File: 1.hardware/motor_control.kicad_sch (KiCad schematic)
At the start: 88 parts, among them IC3 UCC27712QDRQ1, IC4 UCC27712QDRQ1, IC5 UCC27712QDRQ1, J13 2061-603/998-404, J14 2060-452/998-404, J15 2060-453/998-404, Q1 STL130N6F7, Q2 STL130N6F7, Q3 STL130N6F7, Q4 STL130N6F7, Q5 STL130N6F7, Q6 STL130N6F7

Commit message: 중간 저장
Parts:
- removed R153, R154, R155: 0.01R, Resistor_SMD:R_2512_6332Metric, symbol Device:R_Shunt_US
- added R10, R6, R9: 0.01R, Resistor_SMD:R_2512_6332Metric, symbol Device:R_Small_US
- R135, R137, R139: value 2.2/0.25w -> 2.2/0.125w; footprint Resistor_SMD:R_1206_3216Metric -> Resistor_SMD:R_0805_2012Metric
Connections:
- net GNDPWR: now also R10.2, R6.2, R9.2
- net MOTOR_U_SHUNT_P: now also Q2.1 (S_1), Q2.2 (S_2), Q2.3 (S_3), R6.1
- net MOTOR_V_SHUNT_P: now also Q4.1 (S_1), Q4.2 (S_2), Q4.3 (S_3), R9.1
- net MOTOR_W_SHUNT_P: now also Q6.1 (S_1), Q6.2 (S_2), Q6.3 (S_3), R10.1

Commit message: 중간 저장
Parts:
- removed C109, C110, C111: 22uF/100V, Capacitor_SMD:C_Elec_8x10.2, symbol Device:C_Polarized_Small_US
- removed C86, C87: 47uF/50V, Capacitor_SMD:C_Elec_6.3x7.7, symbol Device:C_Polarized_Small_US
- removed R135, R136, R137, R138, R139, R140: 2.2/0.125w, Resistor_SMD:R_0805_2012Metric, symbol Device:R_Small_US
- C88, C89, C90, C91, C92, C93: value 10uF/25V -> 10uF/50V; footprint Capacitor_SMD:C_Elec_4x5.4 -> Capacitor_SMD:C_1206_3216Metric
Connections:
- net 12V: now also C85.1
- net at D18.1: now also IC4.7 (HO), R143.2
- net at IC4.5 (LO), R144.2: now also D19.1
- net at C88.1, C91.1, C97.1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: no longer C85.1
- net at IC3.5 (LO), R142.2: now also D17.1
- net at IC3.7 (HO), R141.2: now also D16.1
- net at IC5.5 (LO), R146.2: now also D21.1
- net at D20.1: now also IC5.7 (HO), R145.2
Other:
- note added: "10uF/50V CL31A106KBHNNNE"
- moved on the sheet: C85, D16, D17, D18, D19, D20, D21, R123, R124, R125

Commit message: 중간 저장
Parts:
- renumbered C90 to C100, C93 to C101, C99 to C102, C105 to C103, C108 to C104, C96 to C105, C102 to C106, C88 to C84, C91 to C85, C97 to C86, C85 to C87, C84 to C88, C103 to C89, C106 to C90, C94 to C91, C100 to C92, C89 to C93, C92 to C94, C98 to C95, C104 to C96, C107 to C97, C95 to C98, C101 to C99, D13 to D12, D16 to D13, D17 to D14, D14 to D15, D18 to D16, D19 to D17, D15 to D18, D20 to D19, D21 to D20, IC3 to IC4, IC4 to IC5, IC5 to IC6, R123 to R119, R132 to R120, R141 to R121, R147 to R122, R126 to R123, R127 to R124, R142 to R125, R148 to R126, R6 to R127, R124 to R128, R133 to R129, R143 to R130, R149 to R131, R128 to R132, R129 to R133, R144 to R134, R150 to R135, R9 to R136, R125 to R137, R134 to R138, R145 to R139, R151 to R140, R130 to R141, R131 to R142, R146 to R143, R152 to R144, R10 to R145, TP12 to TP10, TP14 to TP11, TP11 to TP12, TP15 to TP14, TP10 to TP9

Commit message: 오류 일단 다 잡음
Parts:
- R120, R129, R138: footprint Resistor_SMD:R_0805_2012Metric -> Resistor_SMD:R_1206_3216Metric
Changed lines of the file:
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@@
 			)
 		)
-		(property "Footprint" "Resistor_SMD:R_0805_2012Metric"
+		(property "Footprint" "Resistor_SMD:R_1206_3216Metric"
 			(at 213.36 186.69 0)
 			(effects
@@
 			)
 		)
-		(property "Footprint" "Resistor_SMD:R_0805_2012Metric"
+		(property "Footprint" "Resistor_SMD:R_1206_3216Metric"
 			(at 213.36 110.49 0)
 			(effects
@@
 			)
 		)
-		(property "Footprint" "Resistor_SMD:R_0805_2012Metric"
+		(property "Footprint" "Resistor_SMD:R_1206_3216Metric"
 			(at 212.09 33.02 0)
 			(effects

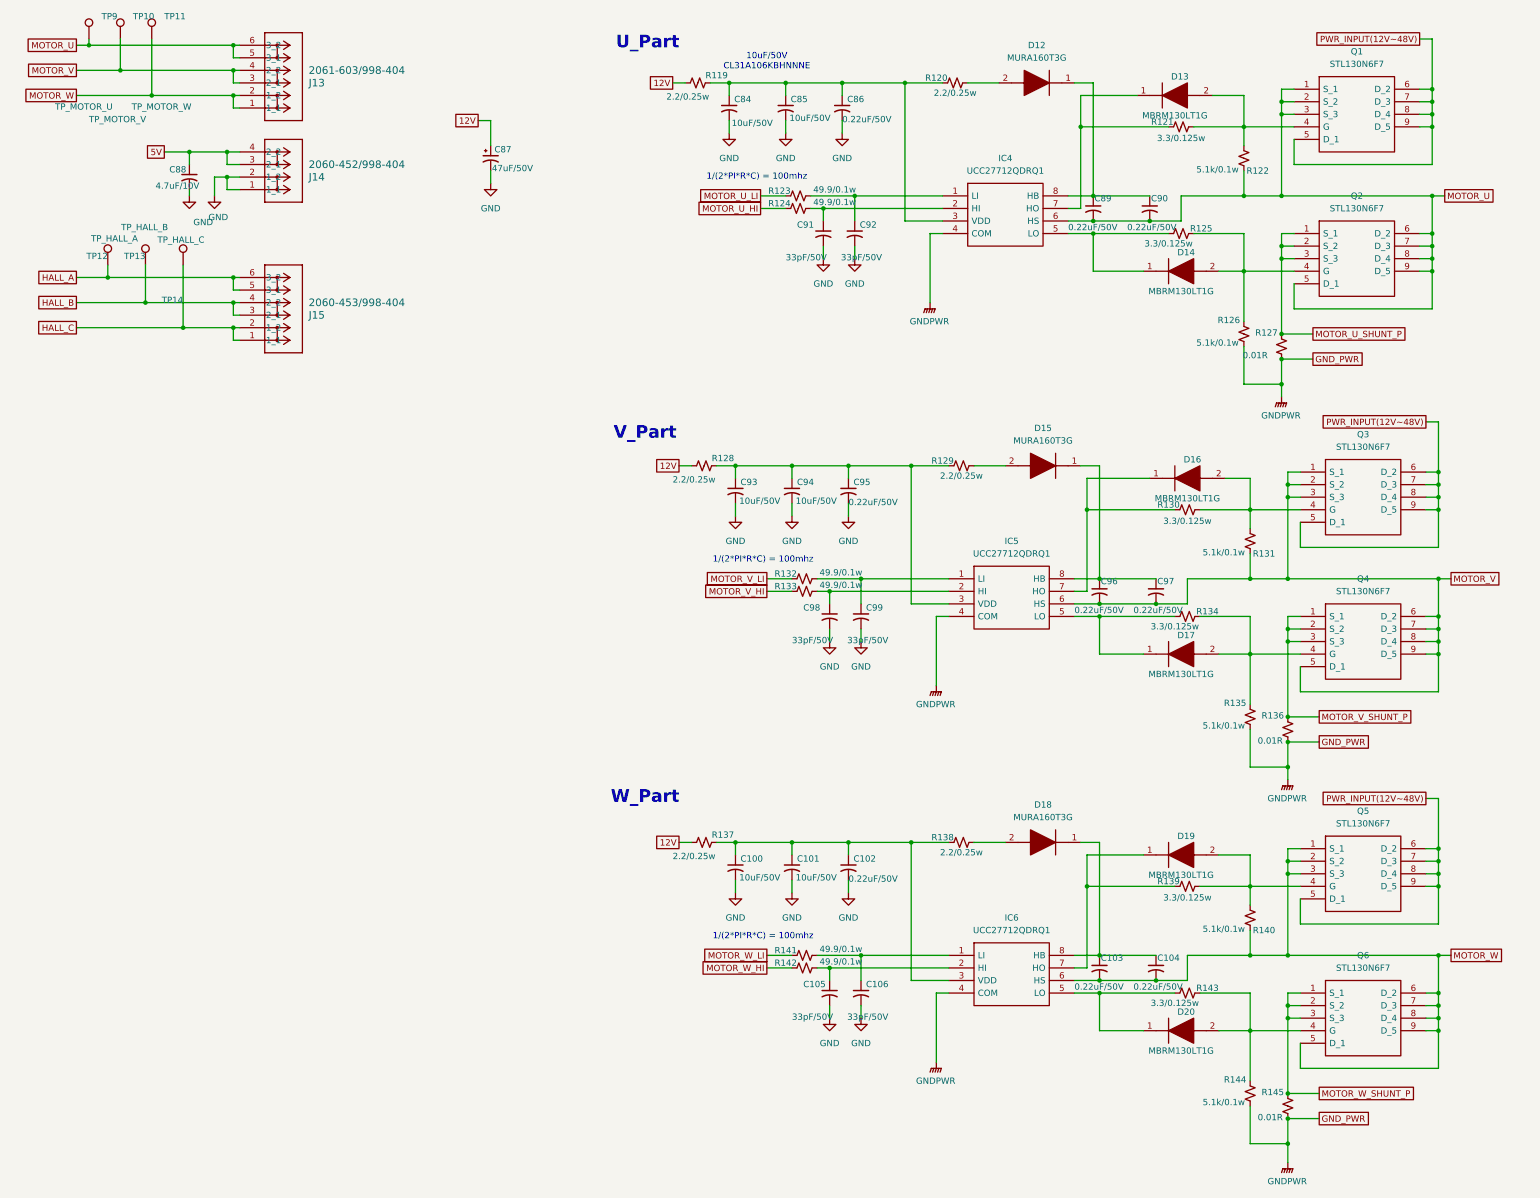
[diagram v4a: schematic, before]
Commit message: 부품 통일 및 필터 부분 캡 선정등 필요해보임
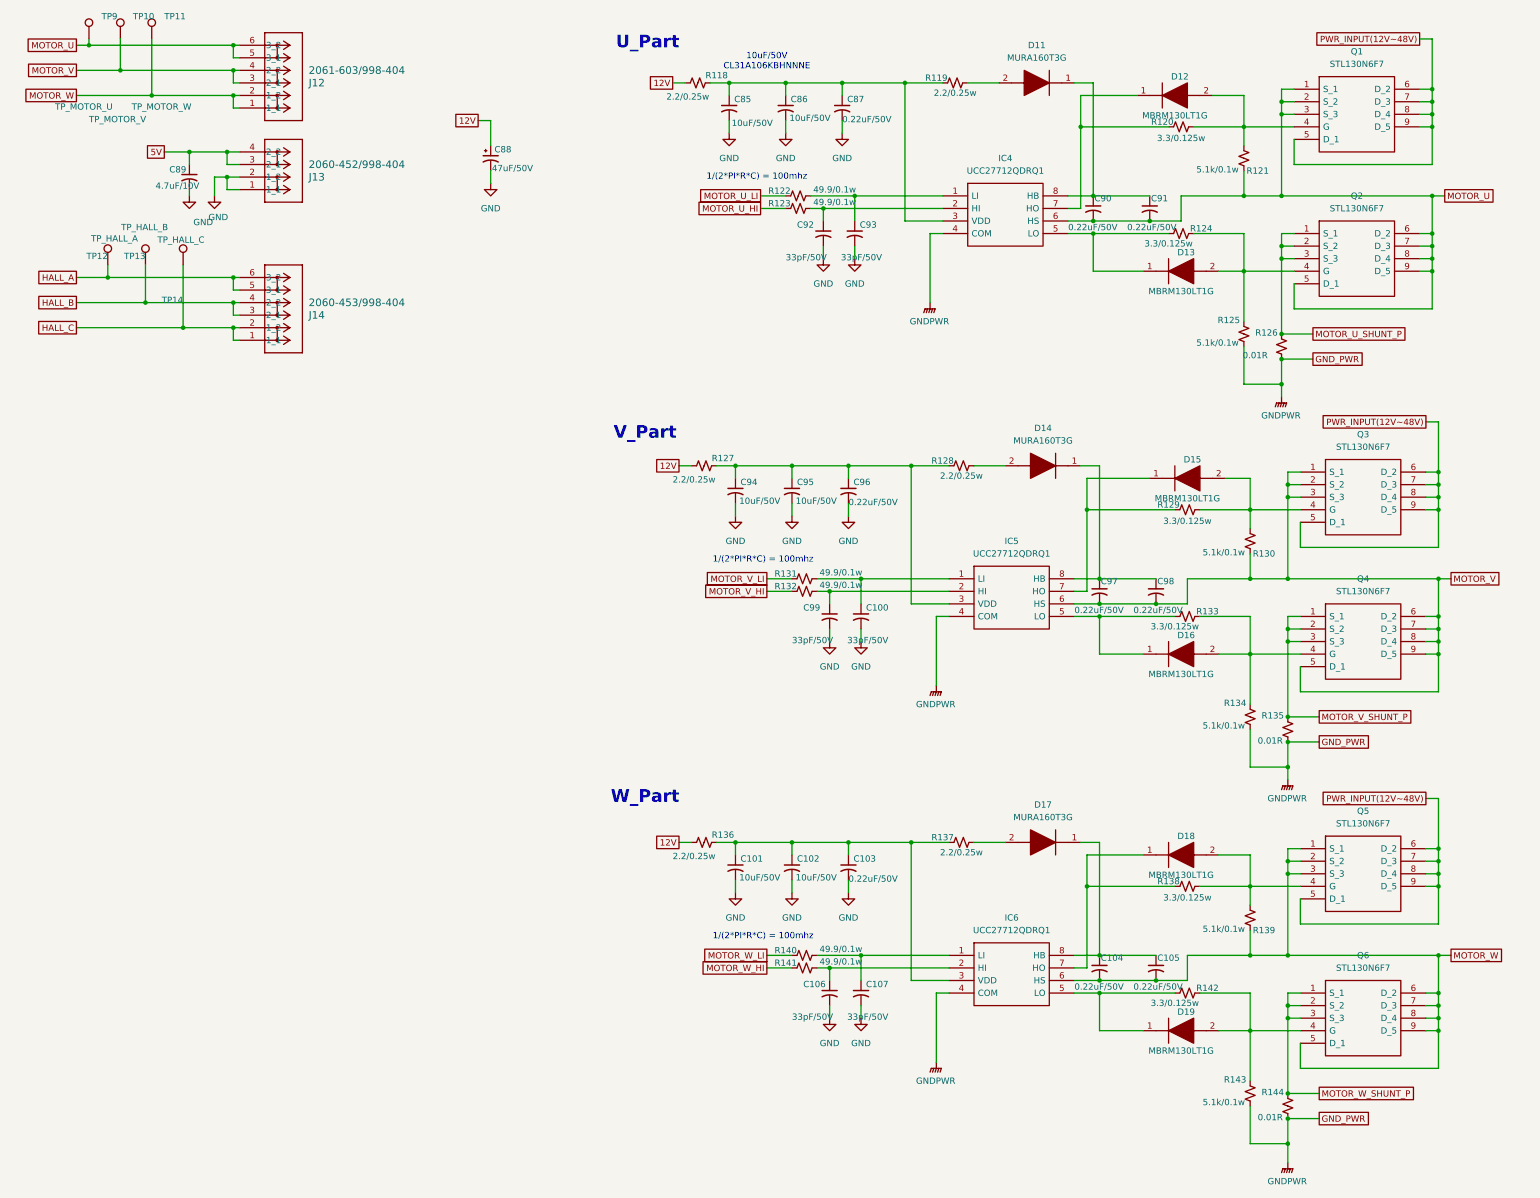
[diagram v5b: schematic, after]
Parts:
- TP10, TP11, TP12, TP13, TP14, TP9: now left out of the parts list
- renumbered C99 to C100, C100 to C101, C101 to C102, C102 to C103, C103 to C104, C104 to C105, C105 to C106, C106 to C107, C84 to C85, C85 to C86, C86 to C87, C87 to C88, C88 to C89, C89 to C90, C90 to C91, C91 to C92, C92 to C93, C93 to C94, C94 to C95, C95 to C96, C96 to C97, C97 to C98, C98 to C99, D12 to D11, D13 to D12, D14 to D13, D15 to D14, D16 to D15, D17 to D16, D18 to D17, D19 to D18, D20 to D19, J13 to J12, J14 to J13, J15 to J14, R119 to R118, R120 to R119, R121 to R120, R122 to R121, R123 to R122, R124 to R123, R125 to R124, R126 to R125, R127 to R126, R128 to R127, R129 to R128, R130 to R129, R131 to R130, R132 to R131, R133 to R132, R134 to R133, R135 to R134, R136 to R135, R137 to R136, R138 to R137, R139 to R138, R140 to R139, R141 to R140, R142 to R141, R143 to R142, R144 to R143, R145 to R144

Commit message: 다시 수정 필요해서 함
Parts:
- C104, C105, C90, C91, C97, C98: footprint Capacitor_SMD:C_0603_1608Metric -> Capacitor_SMD:C_0805_2012Metric
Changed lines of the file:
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@@
 			)
 		)
-		(property "Footprint" "Capacitor_SMD:C_0603_1608Metric"
+		(property "Footprint" "Capacitor_SMD:C_0805_2012Metric"
 			(at 252.73 212.09 0)
 			(effects
@@
 			)
 		)
-		(property "Footprint" "Capacitor_SMD:C_0603_1608Metric"
+		(property "Footprint" "Capacitor_SMD:C_0805_2012Metric"
 			(at 240.03 58.42 0)
 			(effects
@@
 			)
 		)
-		(property "Footprint" "Capacitor_SMD:C_0603_1608Metric"
+		(property "Footprint" "Capacitor_SMD:C_0805_2012Metric"
 			(at 251.46 58.42 0)
 			(effects
@@
 			)
 		)
-		(property "Footprint" "Capacitor_SMD:C_0603_1608Metric"
+		(property "Footprint" "Capacitor_SMD:C_0805_2012Metric"
 			(at 241.3 212.09 0)
 			(effects
@@
 			)
 		)
-		(property "Footprint" "Capacitor_SMD:C_0603_1608Metric"
+		(property "Footprint" "Capacitor_SMD:C_0805_2012Metric"
 			(at 252.73 135.89 0)
 			(effects
@@
 			)
 		)
-		(property "Footprint" "Capacitor_SMD:C_0603_1608Metric"
+		(property "Footprint" "Capacitor_SMD:C_0805_2012Metric"
 			(at 241.3 135.89 0)
 			(effects
